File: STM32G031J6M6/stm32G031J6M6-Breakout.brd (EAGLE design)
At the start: 29.1 x 48.3 mm, 25 parts, among them IC1 LDL112D33R, J2 PWR

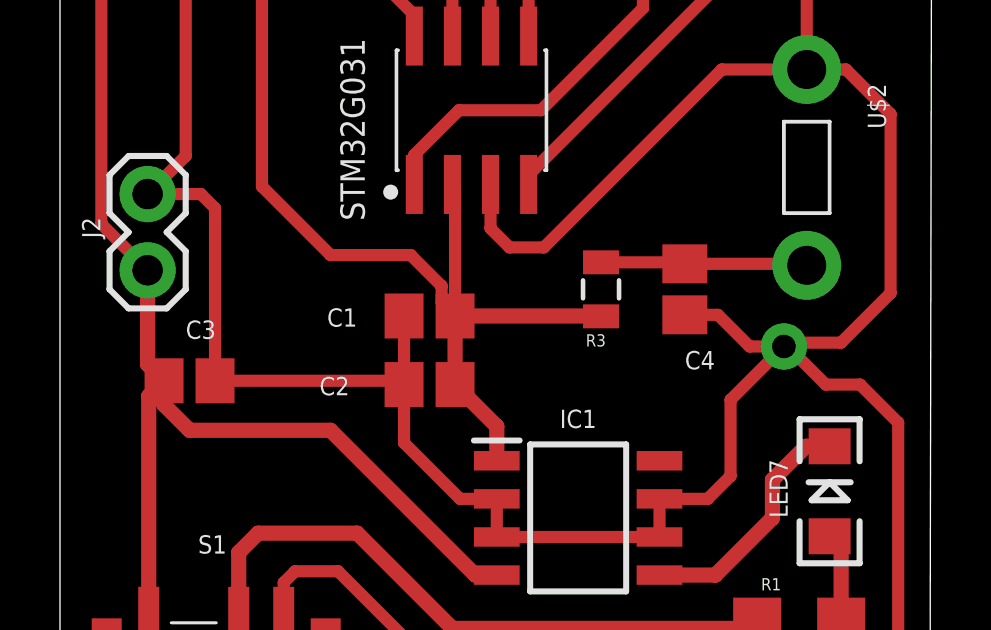
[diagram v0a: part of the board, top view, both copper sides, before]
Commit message: switched packages for caps so I could only work with 1/64 inch bits
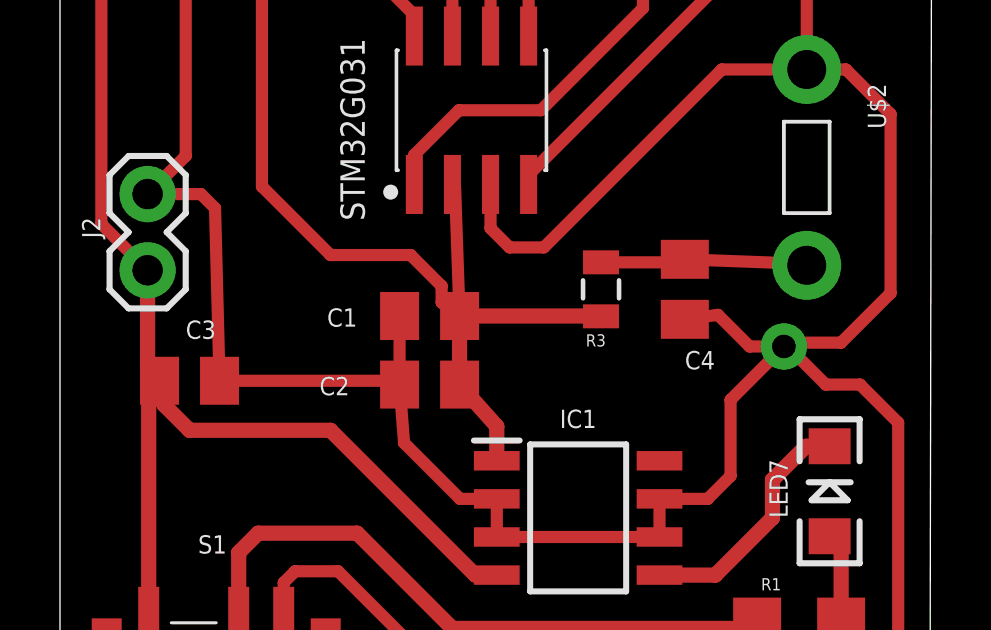
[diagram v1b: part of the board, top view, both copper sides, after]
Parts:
- C1, C2, C3, C4: device passives:C0805 -> passives:C0805K
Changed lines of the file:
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@@
 </autorouter>
 <elements>
-<element name="C1" library="passives" package="C0805" package3d_urn="urn:adsk.eagle:package:8118586/1" value="4.7 uF" x="12.319" y="13.716" smashed="yes" rot="R180">
+<element name="C1" library="passives" package="C0805K" package3d_urn="urn:adsk.eagle:package:8089589/1" value="4.7 uF" x="12.319" y="13.716" smashed="yes" rot="R180">
 <attribute name="NAME" x="9.906" y="13.97" size="0.6096" layer="25" rot="R180"/>
 <attribute name="VALUE" x="16.891" y="14.097" size="0.6096" layer="27" rot="R180"/>
 </element>
-<element name="C2" library="passives" package="C0805" package3d_urn="urn:adsk.eagle:package:8118586/1" value="0.1 uF" x="12.319" y="11.43" smashed="yes" rot="R180">
+<element name="C2" library="passives" package="C0805K" package3d_urn="urn:adsk.eagle:package:8089589/1" value="0.1 uF" x="12.319" y="11.43" smashed="yes" rot="R180">
 <attribute name="NAME" x="9.652" y="11.684" size="0.6096" layer="25" rot="R180"/>
 <attribute name="VALUE" x="16.891" y="11.811" size="0.6096" layer="27" rot="R180"/>
 </element>
-<element name="C3" library="passives" package="C0805" package3d_urn="urn:adsk.eagle:package:8118586/1" value="10 uF" x="4.318" y="11.557" smashed="yes">
+<element name="C3" library="passives" package="C0805K" package3d_urn="urn:adsk.eagle:package:8089589/1" value="10 uF" x="4.318" y="11.557" smashed="yes">
 <attribute name="NAME" x="4.191" y="12.954" size="0.6096" layer="25"/>
 <attribute name="VALUE" x="3.048" y="9.525" size="0.6096" layer="27"/>
 </element>
-<element name="C4" library="passives" package="C0805" package3d_urn="urn:adsk.eagle:package:8118586/1" value="0.1 uF" x="20.828" y="14.605" smashed="yes" rot="R270">
+<element name="C4" library="passives" package="C0805K" package3d_urn="urn:adsk.eagle:package:8089589/1" value="0.1 uF" x="20.828" y="14.605" smashed="yes" rot="R270">
 <attribute name="NAME" x="20.828" y="11.938" size="0.6096" layer="25"/>
 <attribute name="VALUE" x="19.812" y="16.891" size="0.6096" layer="27"/>
@@
 <contactref element="J1" pad="14"/>
 <wire x1="14.56" y1="8.89" x2="14.56" y2="10.039" width="0.508" layer="1"/>
-<wire x1="14.56" y1="10.039" x2="13.169" y2="11.43" width="0.508" layer="1"/>
+<wire x1="14.56" y1="10.039" x2="13.319" y2="11.43" width="0.508" layer="1"/>
 <wire x1="18.023" y1="13.716" x2="18.034" y2="13.705" width="0.4064" layer="1"/>
-<wire x1="13.169" y1="11.43" x2="13.169" y2="13.716" width="0.508" layer="1"/>
-<wire x1="13.169" y1="13.716" x2="18.023" y2="13.716" width="0.508" layer="1"/>
-<wire x1="13.169" y1="13.716" x2="13.169" y2="18.0126" width="0.4064" layer="1"/>
+<wire x1="13.319" y1="11.43" x2="13.319" y2="13.716" width="0.508" layer="1"/>
+<wire x1="13.319" y1="13.716" x2="18.023" y2="13.716" width="0.508" layer="1"/>
+<wire x1="13.319" y1="13.716" x2="13.169" y2="18.0126" width="0.4064" layer="1"/>
 <wire x1="13.169" y1="18.0126" x2="13.081" y2="18.1006" width="0.4064" layer="1"/>
-<wire x1="13.169" y1="13.716" x2="12.72098125" y2="14.16401875" width="0.4064" layer="1"/>
+<wire x1="13.319" y1="13.716" x2="12.72098125" y2="14.16401875" width="0.4064" layer="1"/>
 <wire x1="12.72098125" y1="14.16401875" x2="12.72098125" y2="14.71535" width="0.4064" layer="1"/>
 <wire x1="12.72098125" y1="14.71535" x2="11.68833125" y2="15.748" width="0.4064" layer="1"/>
@@
 <contactref element="J1" pad="13"/>
 <contactref element="J2" pad="2"/>
-<wire x1="5.168" y1="11.557" x2="11.342" y2="11.557" width="0.4064" layer="1"/>
-<wire x1="11.342" y1="11.557" x2="11.469" y2="11.43" width="0.4064" layer="1"/>
-<wire x1="11.469" y1="11.43" x2="11.469" y2="13.716" width="0.4064" layer="1"/>
+<wire x1="5.318" y1="11.557" x2="11.342" y2="11.557" width="0.4064" layer="1"/>
+<wire x1="11.342" y1="11.557" x2="11.319" y2="11.43" width="0.4064" layer="1"/>
+<wire x1="11.319" y1="11.43" x2="11.319" y2="13.716" width="0.4064" layer="1"/>
 <wire x1="14.56" y1="6.35" x2="14.56" y2="7.62" width="0.4064" layer="1"/>
 <wire x1="19.984" y1="6.35" x2="14.56" y2="6.35" width="0.4064" layer="1"/>
 <wire x1="19.984" y1="6.35" x2="19.984" y2="7.62" width="0.4064" layer="1"/>
 <wire x1="14.56" y1="7.62" x2="13.335" y2="7.62" width="0.4064" layer="1"/>
-<wire x1="11.469" y1="9.486" x2="11.469" y2="11.43" width="0.4064" layer="1"/>
+<wire x1="11.469" y1="9.486" x2="11.319" y2="11.43" width="0.4064" layer="1"/>
 <wire x1="13.335" y1="7.62" x2="11.469" y2="9.486" width="0.4064" layer="1"/>
 <wire x1="2.921" y1="17.78" x2="4.699" y2="17.78" width="0.4064" layer="1"/>
-<wire x1="5.168" y1="17.311" x2="5.168" y2="11.557" width="0.4064" layer="1"/>
+<wire x1="5.168" y1="17.311" x2="5.318" y2="11.557" width="0.4064" layer="1"/>
 <wire x1="4.699" y1="17.78" x2="5.168" y2="17.311" width="0.4064" layer="1"/>
 <wire x1="2.921" y1="17.78" x2="4.191" y2="19.05" width="0.4064" layer="1"/>
 <wire x1="4.191" y1="19.05" x2="4.191" y2="27.813" width="0.4064" layer="1"/>
 <via x="24.13" y="12.7" extent="1-16" drill="0.7874"/>
-<wire x1="20.828" y1="13.755" x2="21.932" y2="13.755" width="0.4064" layer="1"/>
+<wire x1="20.828" y1="13.605" x2="21.932" y2="13.755" width="0.4064" layer="1"/>
 <wire x1="22.987" y1="12.7" x2="24.13" y2="12.7" width="0.4064" layer="1"/>
 <wire x1="21.932" y1="13.755" x2="22.987" y2="12.7" width="0.4064" layer="1"/>
@@
 <contactref element="J1" pad="15"/>
 <wire x1="2.921" y1="15.24" x2="2.921" y2="12.104" width="0.508" layer="1"/>
-<wire x1="2.921" y1="12.104" x2="3.468" y2="11.557" width="0.508" layer="1"/>
+<wire x1="2.921" y1="12.104" x2="3.318" y2="11.557" width="0.508" layer="1"/>
 <wire x1="2.957" y1="3.939" x2="2.957" y2="11.046" width="0.508" layer="1"/>
-<wire x1="2.957" y1="11.046" x2="3.468" y2="11.557" width="0.508" layer="1"/>
+<wire x1="2.957" y1="11.046" x2="3.318" y2="11.557" width="0.508" layer="1"/>
 <wire x1="14.56" y1="5.08" x2="13.843" y2="5.08" width="0.508" layer="1"/>
 <wire x1="13.843" y1="5.08" x2="9.017" y2="9.906" width="0.508" layer="1"/>
 <wire x1="9.017" y1="9.906" x2="4.318" y2="9.906" width="0.508" layer="1"/>
-<wire x1="3.468" y1="10.756" x2="3.468" y2="11.557" width="0.508" layer="1"/>
+<wire x1="3.468" y1="10.756" x2="3.318" y2="11.557" width="0.508" layer="1"/>
 <wire x1="4.318" y1="9.906" x2="3.468" y2="10.756" width="0.508" layer="1"/>
 <wire x1="4.191" y1="30.353" x2="1.37921875" y2="27.54121875" width="0.4064" layer="1"/>
@@
 <contactref element="U$2" pad="P$1"/>
 <wire x1="18.034" y1="15.505" x2="20.778" y2="15.505" width="0.4064" layer="1"/>
-<wire x1="20.778" y1="15.505" x2="20.828" y2="15.455" width="0.4064" layer="1"/>
-<wire x1="20.828" y1="15.455" x2="24.8421" y2="15.455" width="0.4064" layer="1"/>
+<wire x1="20.778" y1="15.505" x2="20.828" y2="15.605" width="0.4064" layer="1"/>
+<wire x1="20.828" y1="15.605" x2="24.8421" y2="15.455" width="0.4064" layer="1"/>
 <wire x1="24.8421" y1="15.455" x2="24.892" y2="15.4051" width="0.4064" layer="1"/>
 </signal>

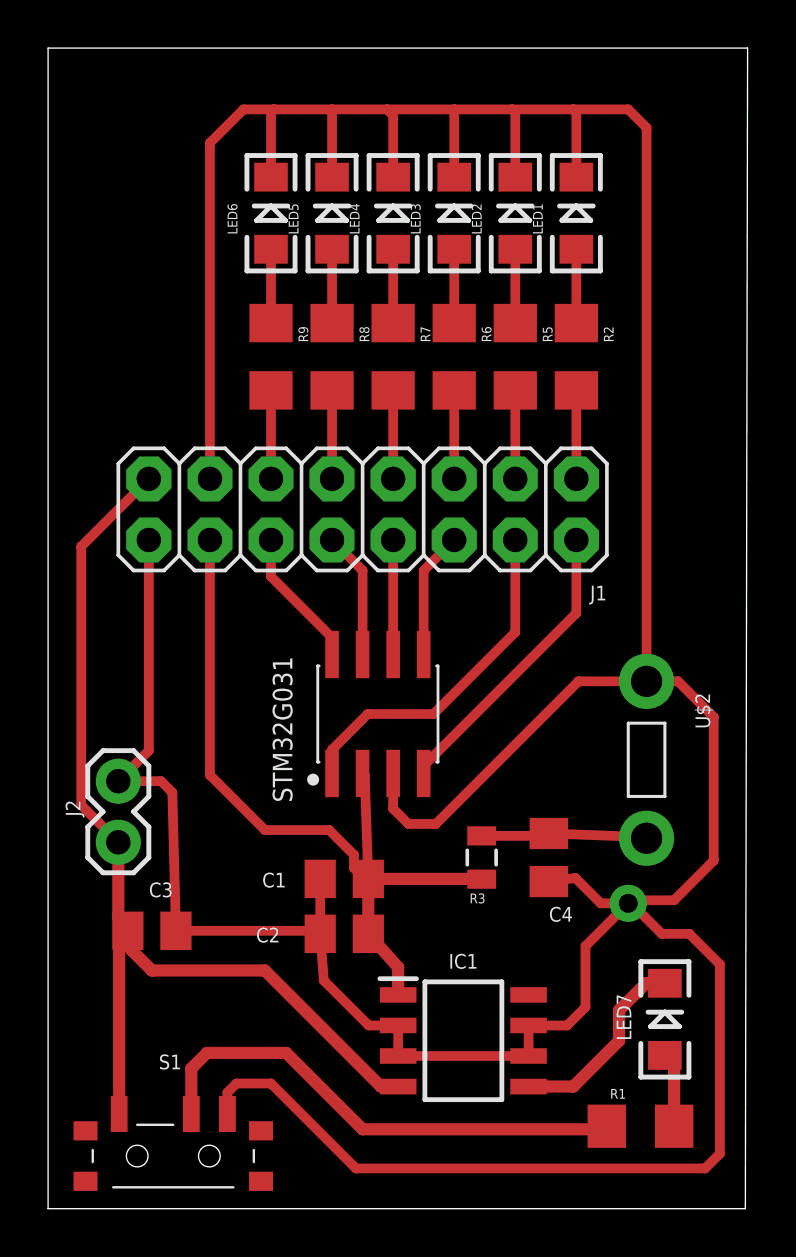
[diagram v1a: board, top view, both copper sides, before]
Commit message: removed reset button as it was wrong AND don't need it
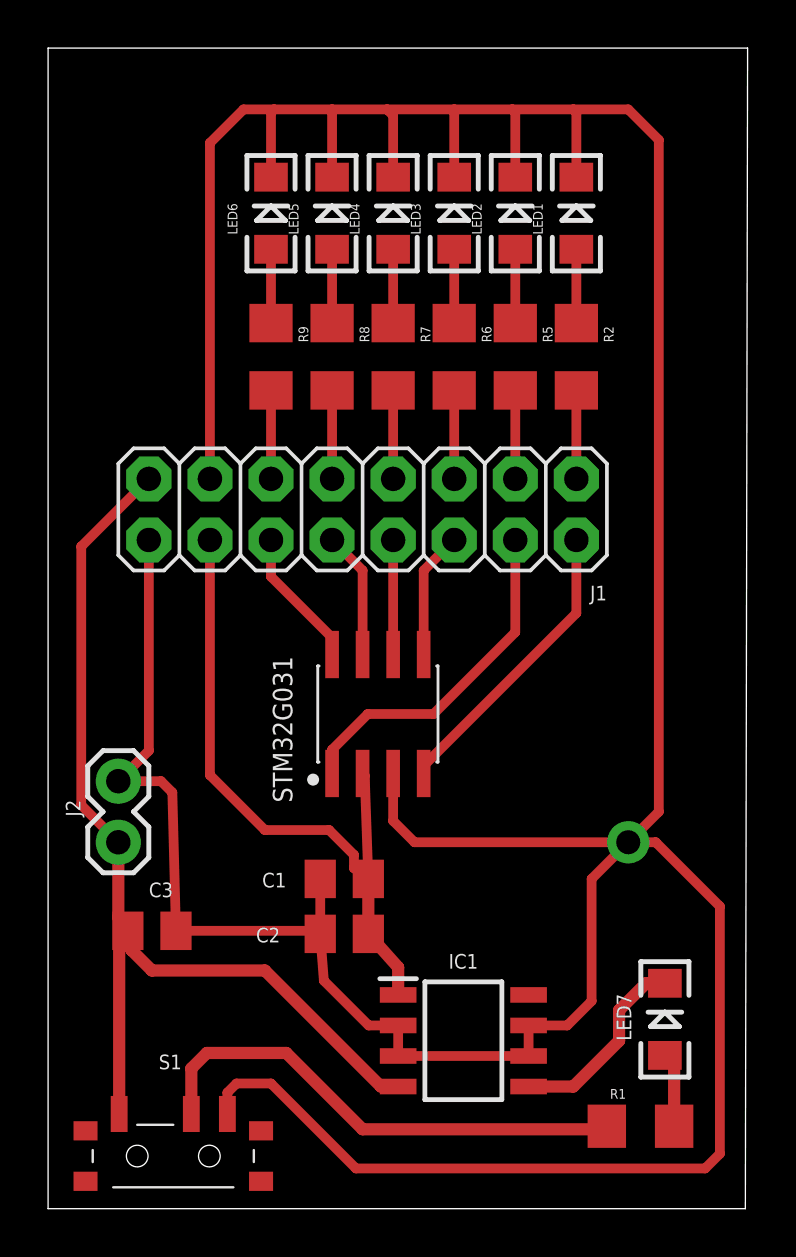
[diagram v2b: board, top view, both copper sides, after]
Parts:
- removed C4: 0.1 uF, passives:C0805K
- removed R3: 10 K, passives:0805
- removed U$2: SWITCH_TACTILETACTILE-2PIN-NARROW, switches:TACTILE-2PIN-NARROW
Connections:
- removed net N$1: C4.1, R3.1, U$2.P$1
- net GND: no longer C4.2, U$2.P$2
- net VDD: no longer R3.2
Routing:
- net GND: track 190.0 -> 182.5 mm
- net N$1: track 6.94 -> 0.00 mm
- net VDD: track 32.9 -> 28.2 mm
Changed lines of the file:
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@@
 <attribute name="VALUE" x="3.048" y="9.525" size="0.6096" layer="27"/>
-</element>
-<element name="C4" library="passives" package="C0805K" package3d_urn="urn:adsk.eagle:package:8089589/1" value="0.1 uF" x="20.828" y="14.605" smashed="yes" rot="R270">
-<attribute name="NAME" x="20.828" y="11.938" size="0.6096" layer="25"/>
-<attribute name="VALUE" x="19.812" y="16.891" size="0.6096" layer="27"/>
 </element>
 <element name="IC1" library="voltage-regulator" package="SOIC127P600X175-8N" value="LDL112D33R" x="17.272" y="6.985" smashed="yes">
@@
 <attribute name="VALUE" x="20.447" y="36.83" size="0.4064" layer="27" rot="R270"/>
 </element>
-<element name="R3" library="passives" package="0805" value="10 K" x="18.034" y="14.605" smashed="yes" rot="R270">
-<attribute name="NAME" x="17.526" y="12.7" size="0.4064" layer="25"/>
-<attribute name="VALUE" x="17.78" y="16.129" size="0.4064" layer="27"/>
-</element>
 <element name="R5" library="passives" package="1206" value="56 R" x="19.431" y="35.433" smashed="yes" rot="R270">
 <attribute name="NAME" x="20.574" y="36.703" size="0.4064" layer="25" rot="R270"/>
@@
 </element>
 <element name="U$1" library="ICs" package="SOIC127P600X175-8N" package3d_urn="urn:adsk.eagle:package:16126582/1" value="STM32G031S08N" x="13.716" y="20.574" smashed="yes" rot="R90"/>
-<element name="U$2" library="switches" package="TACTILE-2PIN-NARROW" value="SWITCH_TACTILETACTILE-2PIN-NARROW" x="24.892" y="18.669" smashed="yes" rot="R270">
-<attribute name="NAME" x="26.924" y="21.463" size="0.6096" layer="25" font="vector" ratio="10" rot="R270"/>
-</element>
 <element name="J2" library="connector" package="1X02" value="PWR" x="2.921" y="15.24" smashed="yes" rot="R90">
 <attribute name="NAME" x="1.3462" y="16.3068" size="0.6096" layer="25" ratio="10" rot="R90"/>
@@
 <contactref element="C2" pad="1"/>
 <contactref element="IC1" pad="1"/>
-<contactref element="R3" pad="2"/>
 <contactref element="J1" pad="14"/>
 <wire x1="14.56" y1="8.89" x2="14.56" y2="10.039" width="0.508" layer="1"/>
 <wire x1="14.56" y1="10.039" x2="13.319" y2="11.43" width="0.508" layer="1"/>
-<wire x1="18.023" y1="13.716" x2="18.034" y2="13.705" width="0.4064" layer="1"/>
 <wire x1="13.319" y1="11.43" x2="13.319" y2="13.716" width="0.508" layer="1"/>
-<wire x1="13.319" y1="13.716" x2="18.023" y2="13.716" width="0.508" layer="1"/>
 <wire x1="13.319" y1="13.716" x2="13.169" y2="18.0126" width="0.4064" layer="1"/>
 <wire x1="13.169" y1="18.0126" x2="13.081" y2="18.1006" width="0.4064" layer="1"/>
@@
 <contactref element="S1" pad="C1"/>
 <contactref element="C3" pad="2"/>
-<contactref element="U$2" pad="P$2"/>
-<contactref element="C4" pad="2"/>
 <contactref element="LED6" pad="C"/>
 <contactref element="LED5" pad="C"/>
@@
 <wire x1="2.921" y1="17.78" x2="4.191" y2="19.05" width="0.4064" layer="1"/>
 <wire x1="4.191" y1="19.05" x2="4.191" y2="27.813" width="0.4064" layer="1"/>
-<via x="24.13" y="12.7" extent="1-16" drill="0.7874"/>
-<wire x1="20.828" y1="13.605" x2="21.932" y2="13.755" width="0.4064" layer="1"/>
-<wire x1="22.987" y1="12.7" x2="24.13" y2="12.7" width="0.4064" layer="1"/>
-<wire x1="21.932" y1="13.755" x2="22.987" y2="12.7" width="0.4064" layer="1"/>
 <wire x1="19.984" y1="7.62" x2="21.59" y2="7.62" width="0.4064" layer="1"/>
-<wire x1="21.59" y1="7.62" x2="22.352" y2="8.382" width="0.4064" layer="1"/>
-<wire x1="22.352" y1="10.922" x2="24.13" y2="12.7" width="0.4064" layer="1"/>
-<wire x1="22.352" y1="8.382" x2="22.352" y2="10.922" width="0.4064" layer="1"/>
-<wire x1="24.13" y1="12.7" x2="24.1935" y2="12.7635" width="0.4064" layer="1"/>
-<wire x1="24.1935" y1="12.7635" x2="24.257" y2="12.827" width="0.4064" layer="1"/>
-<wire x1="24.257" y1="12.827" x2="26.035" y2="12.827" width="0.4064" layer="1"/>
-<wire x1="26.035" y1="12.827" x2="27.686" y2="14.478" width="0.4064" layer="1"/>
-<wire x1="27.686" y1="14.478" x2="27.686" y2="20.447" width="0.4064" layer="1"/>
-<wire x1="27.686" y1="20.447" x2="26.2001" y2="21.9329" width="0.4064" layer="1"/>
-<wire x1="26.2001" y1="21.9329" x2="24.892" y2="21.9329" width="0.4064" layer="1"/>
-<wire x1="24.892" y1="21.9329" x2="24.892" y2="44.958" width="0.4064" layer="1"/>
-<wire x1="24.892" y1="44.958" x2="24.13" y2="45.72" width="0.4064" layer="1"/>
+<wire x1="24.13" y1="45.72" x2="25.4" y2="44.45" width="0.4064" layer="1"/>
 <wire x1="24.13" y1="45.72" x2="21.844" y2="45.72" width="0.4064" layer="1"/>
 <wire x1="21.844" y1="45.72" x2="19.304" y2="45.72" width="0.4064" layer="1"/>
@@
 <wire x1="12.80498125" y1="1.67301875" x2="27.32701875" y2="1.67301875" width="0.4064" layer="1"/>
 <wire x1="27.32701875" y1="1.67301875" x2="27.94" y2="2.286" width="0.4064" layer="1"/>
-<wire x1="27.94" y1="2.286" x2="27.94" y2="10.16" width="0.4064" layer="1"/>
-<wire x1="25.527" y1="11.43" x2="24.1935" y2="12.7635" width="0.4064" layer="1"/>
 <wire x1="7.836" y1="5.207" x2="9.271" y2="5.207" width="0.4064" layer="1"/>
 <wire x1="9.271" y1="5.207" x2="12.80498125" y2="1.67301875" width="0.4064" layer="1"/>
-<wire x1="27.94" y1="10.16" x2="26.67" y2="11.43" width="0.4064" layer="1"/>
-<wire x1="26.67" y1="11.43" x2="25.527" y2="11.43" width="0.4064" layer="1"/>
-<wire x1="14.351" y1="16.637" x2="14.986" y2="16.002" width="0.4064" layer="1"/>
-<wire x1="22.0599" y1="21.9329" x2="24.892" y2="21.9329" width="0.4064" layer="1"/>
-<wire x1="14.351" y1="18.1006" x2="14.351" y2="16.637" width="0.4064" layer="1"/>
-<wire x1="14.986" y1="16.002" x2="16.129" y2="16.002" width="0.4064" layer="1"/>
-<wire x1="16.129" y1="16.002" x2="22.0599" y2="21.9329" width="0.4064" layer="1"/>
+<wire x1="14.351" y1="18.1006" x2="14.351" y2="16.129" width="0.4064" layer="1"/>
+<wire x1="14.351" y1="16.129" x2="15.24" y2="15.24" width="0.4064" layer="1"/>
+<wire x1="21.59" y1="7.62" x2="22.606" y2="8.636" width="0.4064" layer="1"/>
+<wire x1="27.94" y1="2.286" x2="27.94" y2="12.573" width="0.4064" layer="1"/>
+<wire x1="25.4" y1="16.51" x2="25.4" y2="44.45" width="0.4064" layer="1"/>
+<wire x1="25.273" y1="15.24" x2="24.13" y2="15.24" width="0.4064" layer="1"/>
+<wire x1="27.94" y1="12.573" x2="25.273" y2="15.24" width="0.4064" layer="1"/>
+<wire x1="22.606" y1="13.716" x2="24.13" y2="15.24" width="0.4064" layer="1"/>
+<wire x1="22.606" y1="8.636" x2="22.606" y2="13.716" width="0.4064" layer="1"/>
+<wire x1="15.24" y1="15.24" x2="24.13" y2="15.24" width="0.4064" layer="1"/>
+<via x="24.13" y="15.24" extent="1-16" drill="1"/>
+<wire x1="24.13" y1="15.24" x2="25.4" y2="16.51" width="0.4064" layer="1"/>
 </signal>
 <signal name="VIN">
@@
 <wire x1="23.111" y1="3.302" x2="13.081" y2="3.302" width="0.508" layer="1"/>
 </signal>
-<signal name="N$1">
-<contactref element="R3" pad="1"/>
-<contactref element="C4" pad="1"/>
-<contactref element="U$2" pad="P$1"/>
-<wire x1="18.034" y1="15.505" x2="20.778" y2="15.505" width="0.4064" layer="1"/>
-<wire x1="20.778" y1="15.505" x2="20.828" y2="15.605" width="0.4064" layer="1"/>
-<wire x1="20.828" y1="15.605" x2="24.8421" y2="15.455" width="0.4064" layer="1"/>
-<wire x1="24.8421" y1="15.455" x2="24.892" y2="15.4051" width="0.4064" layer="1"/>
-</signal>
 <signal name="N$2">
